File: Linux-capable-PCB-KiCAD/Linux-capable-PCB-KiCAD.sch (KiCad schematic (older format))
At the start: 36 parts, among them U1 A33

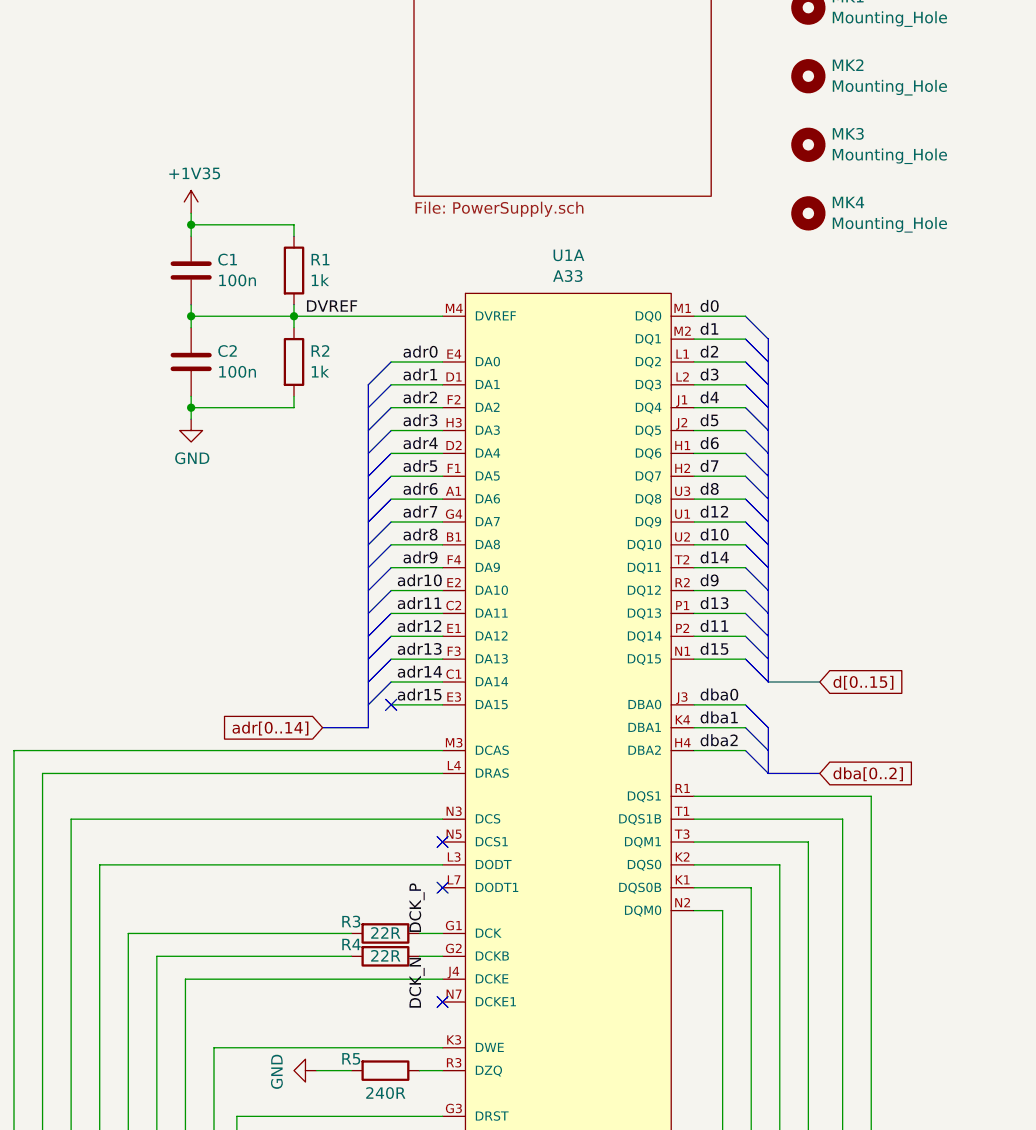
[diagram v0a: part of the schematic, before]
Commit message: CPU and DDR3 connected
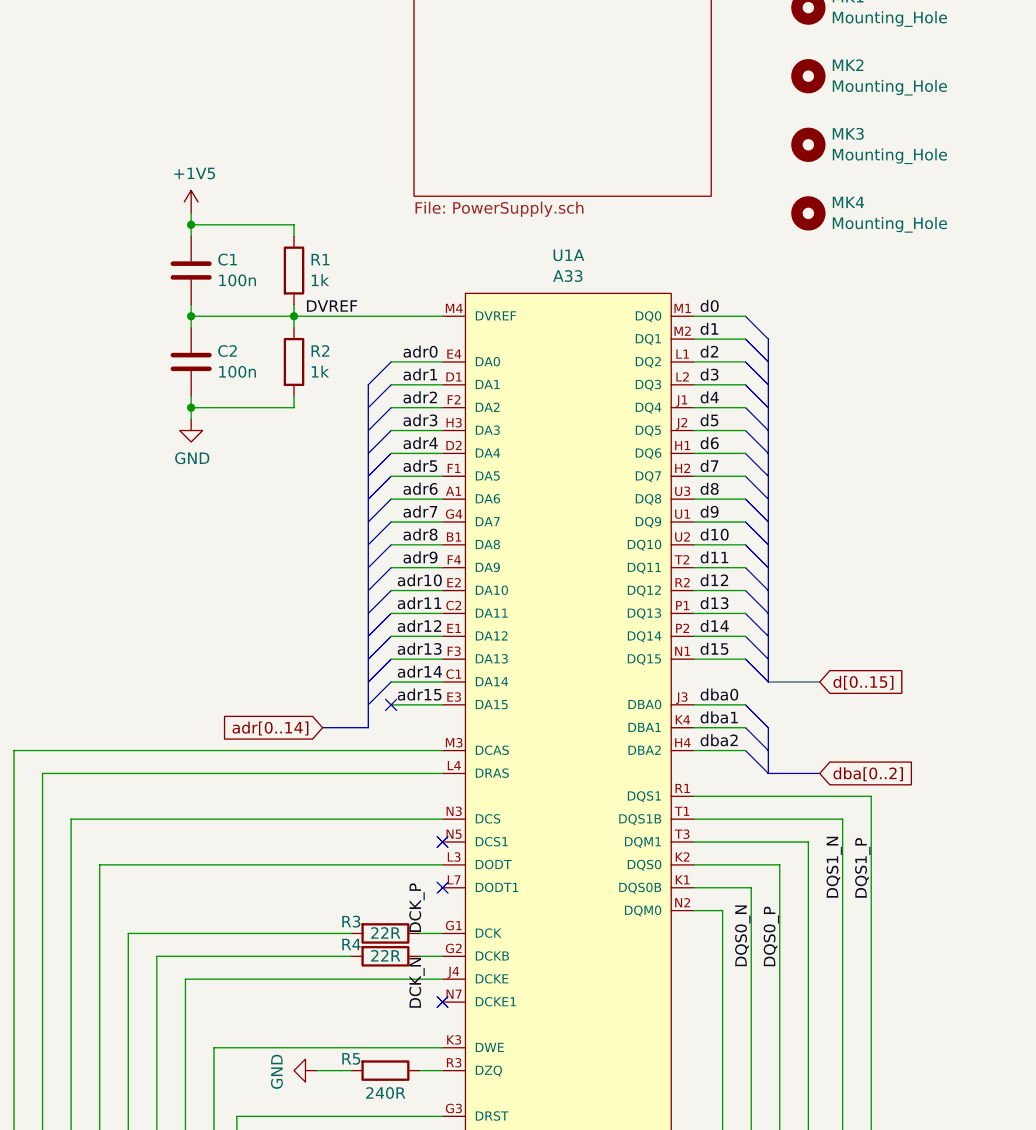
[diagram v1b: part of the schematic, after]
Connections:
- net labels added: +1V5, DQS0_N, DQS0_P, DQS1_N, DQS1_P
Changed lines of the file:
@@
 	1400 2700 1400 2650
 Connection ~ 1400 2650
-$Comp
-L power:+1V35 #PWR0102
-U 1 1 62A1AEBE
-P 1400 1800
-F 0 "#PWR0102" H 1400 1650 50  0001 C CNN
-F 1 "+1V35" H 1415 1973 50  0000 C CNN
-F 2 "" H 1400 1800 50  0001 C CNN
-F 3 "" H 1400 1800 50  0001 C CNN
-	1    1400 1800
-	1    0    0    -1
-$EndComp
 Wire Wire Line
 	1400 1850 1400 1800
@@
 Wire Wire Line
 	3600 2250 3825 2250
-Entry Bus Bus
-	3825 2250 3925 2350
-Entry Bus Bus
-	3825 2350 3925 2450
-Entry Bus Bus
-	3825 2450 3925 2550
-Entry Bus Bus
-	3825 2550 3925 2650
-Entry Bus Bus
-	3825 2650 3925 2750
-Entry Bus Bus
-	3825 2750 3925 2850
-Entry Bus Bus
-	3825 2850 3925 2950
-Entry Bus Bus
-	3825 2950 3925 3050
-Entry Bus Bus
-	3825 3050 3925 3150
-Entry Bus Bus
-	3825 3150 3925 3250
-Entry Bus Bus
-	3825 3250 3925 3350
-Entry Bus Bus
-	3825 3350 3925 3450
-Entry Bus Bus
-	3825 3450 3925 3550
-Entry Bus Bus
-	3825 3550 3925 3650
-Entry Bus Bus
-	3825 3650 3925 3750
-Entry Bus Bus
-	3825 3750 3925 3850
 Wire Wire Line
 	3600 3750 3825 3750
@@
 Wire Wire Line
 	3600 2350 3825 2350
-Wire Bus Line
-	3925 3850 4150 3850
 Wire Wire Line
 	3600 3950 3825 3950
@@
 Wire Bus Line
 	3925 4250 4150 4250
-Text GLabel 4150 3850 2    50   Input ~ 0
-d[0..15]
 Text GLabel 4150 4250 2    50   Input ~ 0
 dba[0..2]
@@
 Text Label 3625 3050 0    50   ~ 0
 d8
-Text Label 3625 3450 0    50   ~ 0
+Text Label 3625 3150 0    50   ~ 0
 d9
 Text Label 3625 3250 0    50   ~ 0
 d10
+Text Label 3625 3350 0    50   ~ 0
+d11
+Text Label 3625 3450 0    50   ~ 0
+d12
 Text Label 3625 3650 0    50   ~ 0
-d11
-Text Label 3625 3150 0    50   ~ 0
-d12
-Text Label 3625 3350 0    50   ~ 0
 d14
 Text Label 3625 3950 0    50   ~ 0
@@
 	1    0    0    -1
 $EndComp
-Wire Bus Line
-	3925 4050 3925 4250
-Wire Bus Line
-	2175 2550 2175 4050
-Wire Bus Line
-	3925 2350 3925 3850
 Text Label 2425 4950 1    50   ~ 0
 DCK_P
@@
 Text Label 3625 3550 0    50   ~ 0
 d13
+$Comp
+L power:+1V5 #PWR0102
+U 1 1 62C64FCF
+P 1400 1800
+F 0 "#PWR0102" H 1400 1650 50  0001 C CNN
+F 1 "+1V5" H 1415 1973 50  0000 C CNN
+F 2 "" H 1400 1800 50  0001 C CNN
+F 3 "" H 1400 1800 50  0001 C CNN
+	1    1400 1800
+	1    0    0    -1
+$EndComp
+Text Label 4375 4800 1    50   ~ 0
+DQS1_P
+Text Label 4250 4800 1    50   ~ 0
+DQS1_N
+Text Label 3975 5100 1    50   ~ 0
+DQS0_P
+Text Label 3850 5100 1    50   ~ 0
+DQS0_N
+Wire Bus Line
+	3925 4050 3925 4250
+Wire Bus Line
+	2175 2550 2175 4050
+Wire Bus Line
+	3925 2350 3925 3850
+Text GLabel 4150 3850 2    50   Input ~ 0
+d[0..15]
+Wire Bus Line
+	3925 3850 4150 3850
+Entry Bus Bus
+	3825 3750 3925 3850
+Entry Bus Bus
+	3825 3650 3925 3750
+Entry Bus Bus
+	3825 3550 3925 3650
+Entry Bus Bus
+	3825 3450 3925 3550
+Entry Bus Bus
+	3825 3350 3925 3450
+Entry Bus Bus
+	3825 3250 3925 3350
+Entry Bus Bus
+	3825 3150 3925 3250
+Entry Bus Bus
+	3825 3050 3925 3150
+Entry Bus Bus
+	3825 2950 3925 3050
+Entry Bus Bus
+	3825 2850 3925 2950
+Entry Bus Bus
+	3825 2750 3925 2850
+Entry Bus Bus
+	3825 2650 3925 2750
+Entry Bus Bus
+	3825 2550 3925 2650
+Entry Bus Bus
+	3825 2450 3925 2550
+Entry Bus Bus
+	3825 2350 3925 2450
+Entry Bus Bus
+	3825 2250 3925 2350
 $EndSCHEMATC
